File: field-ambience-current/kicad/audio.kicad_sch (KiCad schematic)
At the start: 29 parts, among them J6 Speaker L header (2-pin, to S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, J7 Speaker R header (2-pin, to S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, J8 3.5mm TRS Line/Headphone Out 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, U3 PCM5102A I²S DAC (TSSOP-20), U4 PAM8403H Class-D Stereo Amp (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

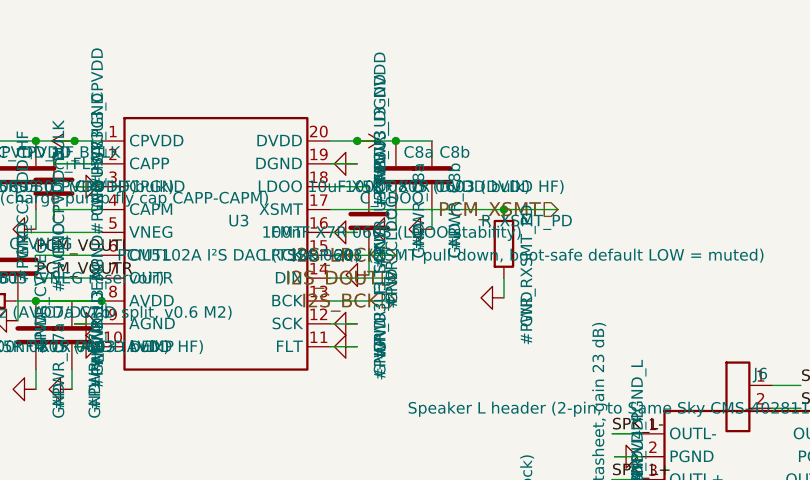
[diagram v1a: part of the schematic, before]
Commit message: fix(pcb): geometric pin-level ERC — 7 copper shorts, 4 open circuits, boost loop instability (r18.80) (#92)
Headless geometric ERC (every pin anchor vs every wire segment, union-find
net build, hier-label/root-pin matching) over all 7 sheets found 12 real
defects; each verified in generator source and fixed there.

Copper shorts (pin/label anchors landing on foreign wires):
- power_tree: USB D+ AND D- hard-shorted to +5V — the U5 LDO block sat in
  the USB data corridor (EN pin on the DP wire, IN pin on the DM wire,
  rail drop overlapping the ESD VBUS wire). Block moved to (130,130).
- mcp: I2C_SCL shorted to GND — C5's GND pin landed exactly on the SCL
  wire (VDD pin 9 and SCL pin 12 are exactly 3 grid rows = 7.62mm apart,
  the cap's pin pitch). Entire I2C bus (U2+U6+U10) was dead. C5/C5b moved.
- audio: PCM_XSMT and I2S_LRCK shorted to GND (same 7.62mm trap, C8a/C8b
  and C_LDOO) — DAC permanently muted / no word clock. Caps flipped up.
- stm32: BOOT0 permanently HIGH twice over (+3V3 flag placed on the BOOT0
  node point; SW_BOOT wire drawn through its own pin-2 anchor) — MCU would
  always enter the ROM bootloader, never firmware.
- stm32: VDDA copper-tied to VDD (pin-21 stub drawn through the VDD pin-100
  anchor), bypassing FB2.
- battery: U8_SW_NODE label sat on the SW/BOOT wire crossing, merging the
  bootstrap net with the switch node (C_BOOT ineffective).

Open circuits:
- lcd: J3 LCD header — all 8 pins floating (wiring assumed KiCad-standard
  pins at -5.08 left; custom lib has pins at +3.81 right). J3 rotated 180.
- stm32: J4 SWD header — all 3 pins floating (same assumption). Board was
  unprogrammable.
- stm32: FB2 rotated 90 off its wires — both pins floating (VDDA had no
  intended supply path).
- stm32: lib_symbols entry lacked the MCU: prefix — KiCad cannot resolve
  U1 at all (exact lib_id match required).

Boost control loop (TPS61089, TI SLVSD38C eqs 15/17/18, validated by
reproducing TI's own 9V/2A reference values):
- R_COMP 22k -> 6.2k (n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
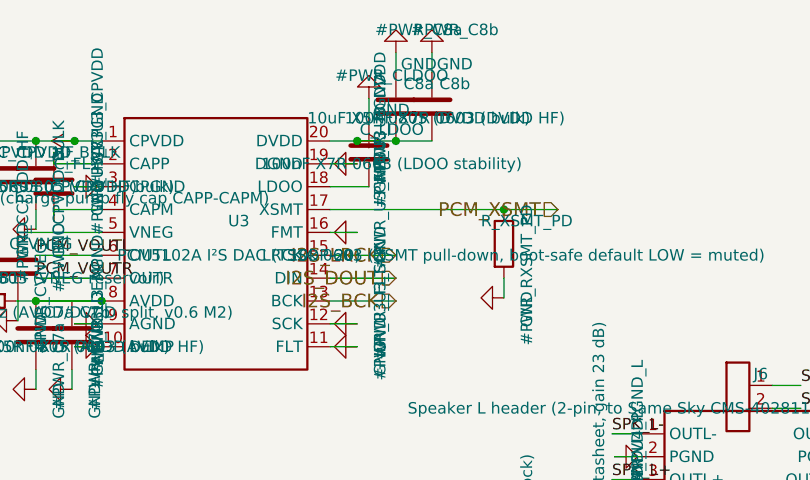
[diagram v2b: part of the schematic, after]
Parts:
- C7a, C8a, C_CPVDD_BULK: MPN CL21A106KOQNNNE -> CL21A106KAYNNNE
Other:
- moved on the sheet: C8a, C8b, C_LDOO
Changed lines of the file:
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@@
       (property "Datasheet" "~" (at 80 92.38 0)
         (effects (font (size 1.27 1.27)) hide))
-      (property "MPN" "CL21A106KOQNNNE" (at 82.54 96.19 0)
+      (property "MPN" "CL21A106KAYNNNE" (at 82.54 96.19 0)
         (effects (font (size 1.27 1.27)) hide))
       (property "LCSC" "C15850" (at 82.54 97.46 0)
@@
       (property "Datasheet" "~" (at 80 110.16 0)
         (effects (font (size 1.27 1.27)) hide))
-      (property "MPN" "CL21A106KOQNNNE" (at 82.54 113.97 0)
+      (property "MPN" "CL21A106KAYNNNE" (at 82.54 113.97 0)
         (effects (font (size 1.27 1.27)) hide))
       (property "LCSC" "C15850" (at 82.54 115.24 0)
@@
       (project "field_ambience"
         (path "/66fcdc89-be06-4d61-a855-abf9641d963c" (reference "#PWR_RXSMT_PD") (unit 1)))))
-  (symbol (lib_id "Device:C") (at 117 97.46 0) (unit 1)
-    (in_bom yes) (on_board yes) (dnp no)
-      (property "Reference" "C_LDOO" (at 119.54 94.91999999999999 0)
-        (effects (font (size 1.27 1.27))))
-      (property "Value" "100nF X7R 0603 (LDOO stability)" (at 119.54 98.72999999999999 0)
-        (effects (font (size 1.27 1.27))))
-      (property "Footprint" "Capacitor_SMD:C_0603_1608Metric" (at 117 97.46 0)
-        (effects (font (size 1.27 1.27)) hide))
-      (property "Datasheet" "~" (at 117 97.46 0)
-        (effects (font (size 1.27 1.27)) hide))
-      (property "MPN" "CC0603KRX7R9BB104" (at 119.54 101.27 0)
-        (effects (font (size 1.27 1.27)) hide))
-      (property "LCSC" "C14663" (at 119.54 102.53999999999999 0)
+  (symbol (lib_id "Device:C") (at 117 89.83999999999999 180) (unit 1)
+    (in_bom yes) (on_board yes) (dnp no)
+      (property "Reference" "C_LDOO" (at 119.54 87.29999999999998 0)
+        (effects (font (size 1.27 1.27))))
+      (property "Value" "100nF X7R 0603 (LDOO stability)" (at 119.54 91.10999999999999 0)
+        (effects (font (size 1.27 1.27))))
+      (property "Footprint" "Capacitor_SMD:C_0603_1608Metric" (at 117 89.83999999999999 0)
+        (effects (font (size 1.27 1.27)) hide))
+      (property "Datasheet" "~" (at 117 89.83999999999999 0)
+        (effects (font (size 1.27 1.27)) hide))
+      (property "MPN" "CC0603KRX7R9BB104" (at 119.54 93.64999999999999 0)
+        (effects (font (size 1.27 1.27)) hide))
+      (property "LCSC" "C14663" (at 119.54 94.91999999999999 0)
         (effects (font (size 1.27 1.27)) hide))
     (instances
       (project "field_ambience"
         (path "/66fcdc89-be06-4d61-a855-abf9641d963c" (reference "C_LDOO") (unit 1)))))
-  (symbol (lib_id "Power:GND") (at 117 103.46 270) (unit 1)
-    (in_bom yes) (on_board yes) (dnp no)
-      (property "Reference" "#PWR_CLDOO" (at 119.54 100.91999999999999 0)
-        (effects (font (size 1.27 1.27))))
-      (property "Value" "GND" (at 119.54 104.72999999999999 0)
-        (effects (font (size 1.27 1.27))))
-      (property "Footprint" "" (at 117 103.46 0)
-        (effects (font (size 1.27 1.27)) hide))
-      (property "Datasheet" "~" (at 117 103.46 0)
+  (symbol (lib_id "Power:GND") (at 117 83.83999999999999 180) (unit 1)
+    (in_bom yes) (on_board yes) (dnp no)
+      (property "Reference" "#PWR_CLDOO" (at 119.54 81.29999999999998 0)
+        (effects (font (size 1.27 1.27))))
+      (property "Value" "GND" (at 119.54 85.10999999999999 0)
+        (effects (font (size 1.27 1.27))))
+      (property "Footprint" "" (at 117 83.83999999999999 0)
+        (effects (font (size 1.27 1.27)) hide))
+      (property "Datasheet" "~" (at 117 83.83999999999999 0)
         (effects (font (size 1.27 1.27)) hide))
     (instances
@@
       (project "field_ambience"
         (path "/66fcdc89-be06-4d61-a855-abf9641d963c" (reference "#PWR_U3_DVDD") (unit 1)))))
-  (symbol (lib_id "Device:C") (at 120 92.38 0) (unit 1)
-    (in_bom yes) (on_board yes) (dnp no)
-      (property "Reference" "C8a" (at 122.54 89.83999999999999 0)
-        (effects (font (size 1.27 1.27))))
-      (property "Value" "10uF X5R 0805 (DVDD bulk)" (at 122.54 93.64999999999999 0)
-        (effects (font (size 1.27 1.27))))
-      (property "Footprint" "Capacitor_SMD:C_0805_2012Metric" (at 120 92.38 0)
-        (effects (font (size 1.27 1.27)) hide))
-      (property "Datasheet" "~" (at 120 92.38 0)
-        (effects (font (size 1.27 1.27)) hide))
-      (property "MPN" "CL21A106KOQNNNE" (at 122.54 96.19 0)
-        (effects (font (size 1.27 1.27)) hide))
-      (property "LCSC" "C15850" (at 122.54 97.46 0)
+  (symbol (lib_id "Device:C") (at 120 84.75999999999999 180) (unit 1)
+    (in_bom yes) (on_board yes) (dnp no)
+      (property "Reference" "C8a" (at 122.54 82.21999999999998 0)
+        (effects (font (size 1.27 1.27))))
+      (property "Value" "10uF X5R 0805 (DVDD bulk)" (at 122.54 86.02999999999999 0)
+        (effects (font (size 1.27 1.27))))
+      (property "Footprint" "Capacitor_SMD:C_0805_2012Metric" (at 120 84.75999999999999 0)
+        (effects (font (size 1.27 1.27)) hide))
+      (property "Datasheet" "~" (at 120 84.75999999999999 0)
+        (effects (font (size 1.27 1.27)) hide))
+      (property "MPN" "CL21A106KAYNNNE" (at 122.54 88.57 0)
+        (effects (font (size 1.27 1.27)) hide))
+      (property "LCSC" "C15850" (at 122.54 89.83999999999999 0)
         (effects (font (size 1.27 1.27)) hide))
     (instances
       (project "field_ambience"
         (path "/66fcdc89-be06-4d61-a855-abf9641d963c" (reference "C8a") (unit 1)))))
-  (symbol (lib_id "Power:GND") (at 120 98.38 270) (unit 1)
-    (in_bom yes) (on_board yes) (dnp no)
-      (property "Reference" "#PWR_C8a" (at 122.54 95.83999999999999 0)
-        (effects (font (size 1.27 1.27))))
-      (property "Value" "GND" (at 122.54 99.64999999999999 0)
-        (effects (font (size 1.27 1.27))))
-      (property "Footprint" "" (at 120 98.38 0)
-        (effects (font (size 1.27 1.27)) hide))
-      (property "Datasheet" "~" (at 120 98.38 0)
+  (symbol (lib_id "Power:GND") (at 120 78.75999999999999 180) (unit 1)
+    (in_bom yes) (on_board yes) (dnp no)
+      (property "Reference" "#PWR_C8a" (at 122.54 76.21999999999998 0)
+        (effects (font (size 1.27 1.27))))
+      (property "Value" "GND" (at 122.54 80.02999999999999 0)
+        (effects (font (size 1.27 1.27))))
+      (property "Footprint" "" (at 120 78.75999999999999 0)
+        (effects (font (size 1.27 1.27)) hide))
+      (property "Datasheet" "~" (at 120 78.75999999999999 0)
         (effects (font (size 1.27 1.27)) hide))
     (instances
       (project "field_ambience"
         (path "/66fcdc89-be06-4d61-a855-abf9641d963c" (reference "#PWR_C8a") (unit 1)))))
-  (symbol (lib_id "Device:C") (at 124 92.38 0) (unit 1)
-    (in_bom yes) (on_board yes) (dnp no)
-      (property "Reference" "C8b" (at 126.54 89.83999999999999 0)
-        (effects (font (size 1.27 1.27))))
-      (property "Value" "100nF X7R 0603 (DVDD HF)" (at 126.54 93.64999999999999 0)
-        (effects (font (size 1.27 1.27))))
-      (property "Footprint" "Capacitor_SMD:C_0603_1608Metric" (at 124 92.38 0)
-        (effects (font (size 1.27 1.27)) hide))
-      (property "Datasheet" "~" (at 124 92.38 0)
-        (effects (font (size 1.27 1.27)) hide))
-      (property "MPN" "CC0603KRX7R9BB104" (at 126.54 96.19 0)
-        (effects (font (size 1.27 1.27)) hide))
-      (property "LCSC" "C14663" (at 126.54 97.46 0)
+  (symbol (lib_id "Device:C") (at 124 84.75999999999999 180) (unit 1)
+    (in_bom yes) (on_board yes) (dnp no)
+      (property "Reference" "C8b" (at 126.54 82.21999999999998 0)
+        (effects (font (size 1.27 1.27))))
+      (property "Value" "100nF X7R 0603 (DVDD HF)" (at 126.54 86.02999999999999 0)
+        (effects (font (size 1.27 1.27))))
+      (property "Footprint" "Capacitor_SMD:C_0603_1608Metric" (at 124 84.75999999999999 0)
+        (effects (font (size 1.27 1.27)) hide))
+      (property "Datasheet" "~" (at 124 84.75999999999999 0)
+        (effects (font (size 1.27 1.27)) hide))
+      (property "MPN" "CC0603KRX7R9BB104" (at 126.54 88.57 0)
+        (effects (font (size 1.27 1.27)) hide))
+      (property "LCSC" "C14663" (at 126.54 89.83999999999999 0)
         (effects (font (size 1.27 1.27)) hide))
     (instances
       (project "field_ambience"
         (path "/66fcdc89-be06-4d61-a855-abf9641d963c" (reference "C8b") (unit 1)))))
-  (symbol (lib_id "Power:GND") (at 124 98.38 270) (unit 1)
-    (in_bom yes) (on_board yes) (dnp no)
-      (property "Reference" "#PWR_C8b" (at 126.54 95.83999999999999 0)
-        (effects (font (size 1.27 1.27))))
-      (property "Value" "GND" (at 126.54 99.64999999999999 0)
-        (effects (font (size 1.27 1.27))))
-      (property "Footprint" "" (at 124 98.38 0)
-        (effects (font (size 1.27 1.27)) hide))
-      (property "Datasheet" "~" (at 124 98.38 0)
+  (symbol (lib_id "Power:GND") (at 124 78.75999999999999 180) (unit 1)
+    (in_bom yes) (on_board yes) (dnp no)
+      (property "Reference" "#PWR_C8b" (at 126.54 76.21999999999998 0)
+        (effects (font (size 1.27 1.27))))
+      (property "Value" "GND" (at 126.54 80.02999999999999 0)
+        (effects (font (size 1.27 1.27))))
+      (property "Footprint" "" (at 124 78.75999999999999 0)
+        (effects (font (size 1.27 1.27)) hide))
+      (property "Datasheet" "~" (at 124 78.75999999999999 0)
         (effects (font (size 1.27 1.27)) hide))
     (instances
@@
     (stroke (width 0) (type default))
 )
-  (wire (pts (xy 117 101.27) (xy 117 103.46))
+  (wire (pts (xy 117 86.02999999999999) (xy 117 83.83999999999999))
     (stroke (width 0) (type default))
 )
@@
     (stroke (width 0) (type default))
 )
-  (wire (pts (xy 120 96.19) (xy 120 98.38))
+  (wire (pts (xy 120 80.94999999999999) (xy 120 78.75999999999999))
     (stroke (width 0) (type default))
 )
@@
     (stroke (width 0) (type default))
 )
-  (wire (pts (xy 124 96.19) (xy 124 98.38))
-    (stroke (width 0) (type default))
-)
+  (wire (pts (xy 124 80.94999999999999) (xy 124 78.75999999999999))
+    (stroke (width 0) (type default))
+)
